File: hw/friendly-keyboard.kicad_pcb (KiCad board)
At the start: 6 copper layers, 35 x 50 mm, 73 parts, among them J1 Conn_Coaxial, J2 Conn_01x02, J3 USB_C_Receptacle_USB2.0, J4 Left Mezzanine, J5 Left Mezzanine, U1 NRF21540-QDAA-R, U2 LTC3411AEDD, U3 MAX77751CEFG+, U4 NRF5340-QKAA-R7, U5 W25Q32JVZP, U6 PCAL6524, U7 PCAL6524, U8 PCAL6524, Y1 32MHz-ECS-320-8-37B2-7KM-TR, Y2 32.768kHz

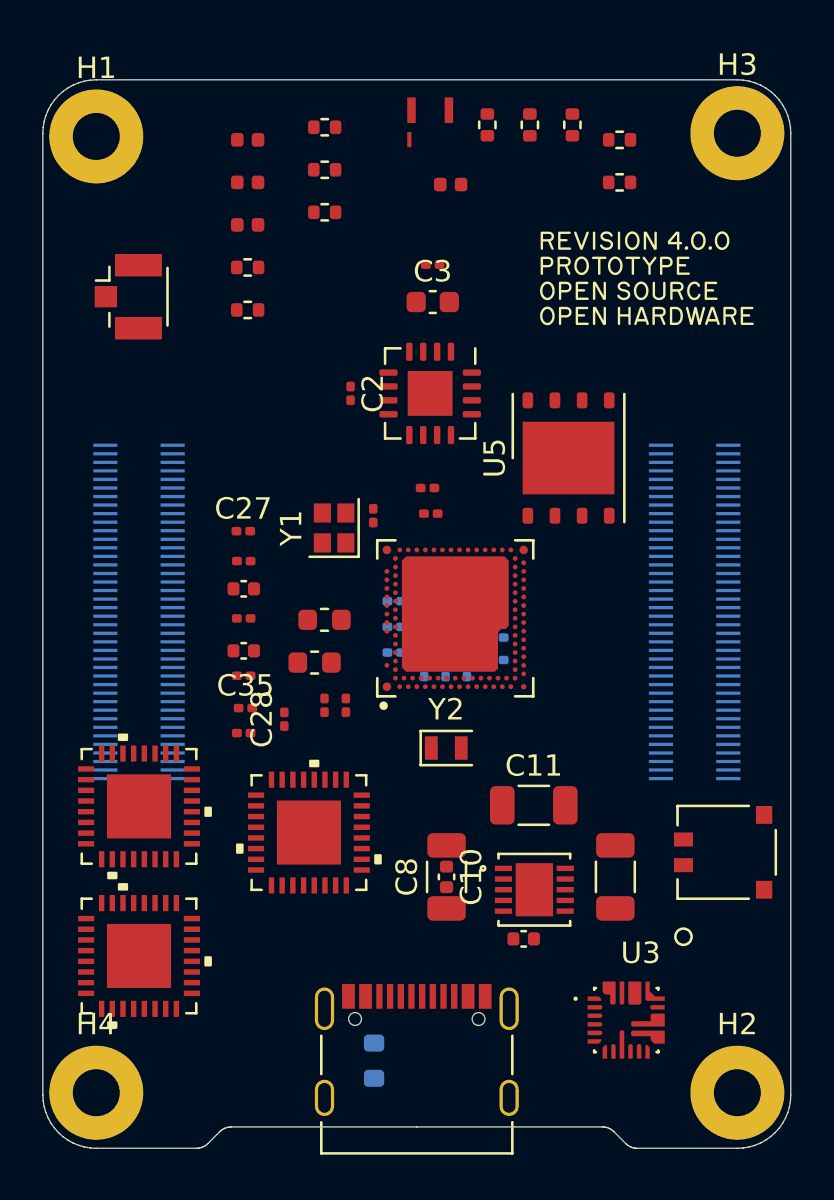
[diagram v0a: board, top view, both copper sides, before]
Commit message: 
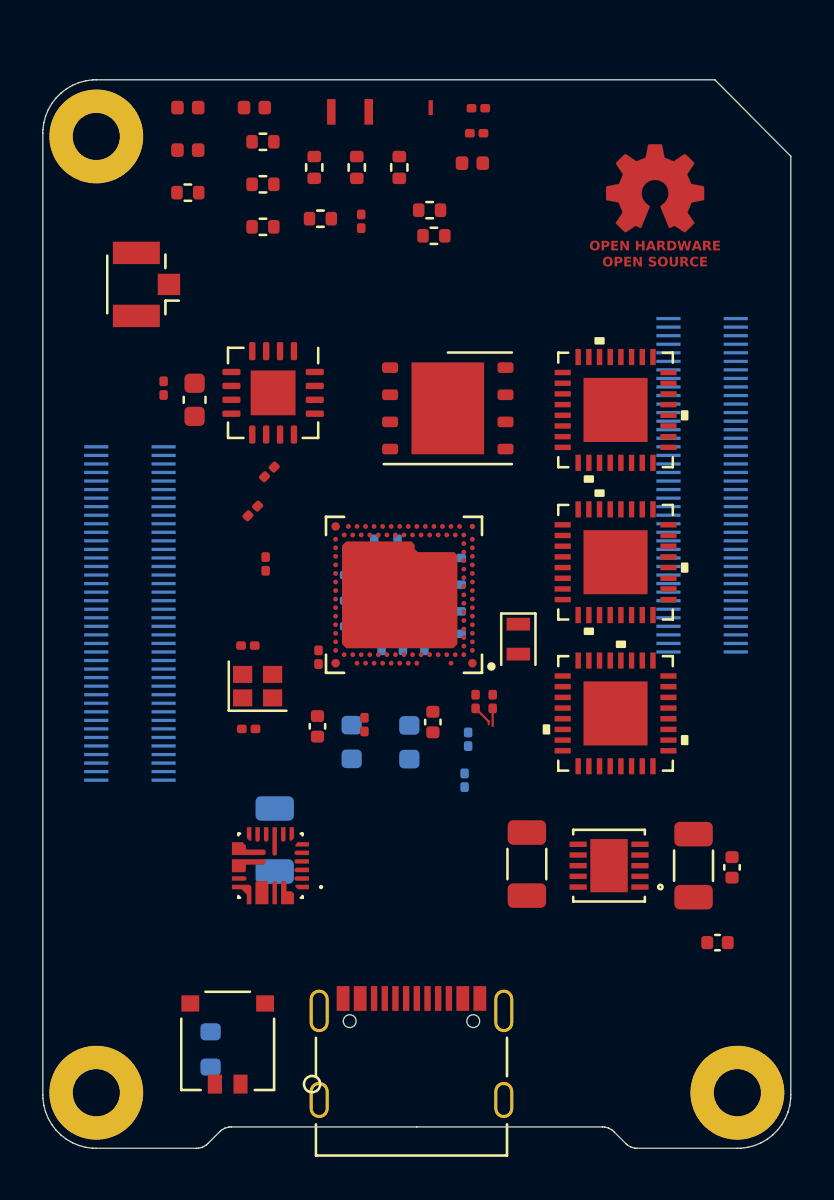
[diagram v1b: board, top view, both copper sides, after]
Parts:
- removed H3: H4, MountingHole:MountingHole_2.2mm_M2_Pad
- added REF**: OSHW-Logo2_7.3x6mm_Copper, Symbol:OSHW-Logo2_7.3x6mm_Copper, F.Cu at (161.2, 130.9)
- C11, C32, C33, L5, L6: moved to B.Cu
- C19: moved to F.Cu
- moved U7 33.9 mm to (159.3, 140.5)
- moved C34 30.1 mm to (152.8, 127.6)
- moved C35 30.1 mm to (152.9, 126.4)
- moved U8 25.1 mm to (159.3, 147.7)
- moved J2 25.0 mm to (141.2, 170.1), turned to 180 degrees
- moved U3 18.2 mm to (143.2, 161.9), turned to 180 degrees
- moved U6 15.4 mm to (159.3, 154.7)
- moved C10 13.0 mm to (164.1, 165.5), turned to 180 degrees
- moved C32 12.8 mm to (152.2, 157.9), turned to 90 degrees
- moved C11 12.2 mm to (143.4, 160.7), turned to 90 degrees
- moved C3 12.0 mm to (139.6, 140.1), turned to -90 degrees
- moved C8 11.6 mm to (163.0, 161.9), turned to -90 degrees
- moved C36 11.6 mm to (142.1, 155.5), turned to 0 degrees
- moved C19 11.0 mm to (142.1, 151.6), turned to 180 degrees
- moved C33 10.9 mm to (152.4, 156.0), turned to 90 degrees
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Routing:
- net (no net): track 0.00 -> 118.6 mm
- net unconnected-(U4G-P0.26/AIN5-PadAL29): track 0.00 -> 17.9 mm
- net unconnected-(U4G-P0.27/AIN6-PadAK30): track 0.00 -> 17.9 mm
- net /Microcontroller/GPIO/NRF_IFX.USB_+: track 0.00 -> 1.00 mm
- net /Microcontroller/GPIO/NRF_IFX.USB_-: track 0.00 -> 0.83 mm
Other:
- outline, holes or cut-outs redrawn
- board text removed: "Chip Antenna"
